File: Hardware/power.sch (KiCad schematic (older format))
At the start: 63 parts, among them IC2 SIP32431DR3-T1GE3, IC3 SIP32431DR3-T1GE3, J2 614105150721, J3 B2B-XH-A, J4 POWER ON, Q2 FDC638P, Q3 IRLML6244TRPBF, Q4 BSS138, Q5 BSS138, U10 TPS63900DSKR, U8 TP4056

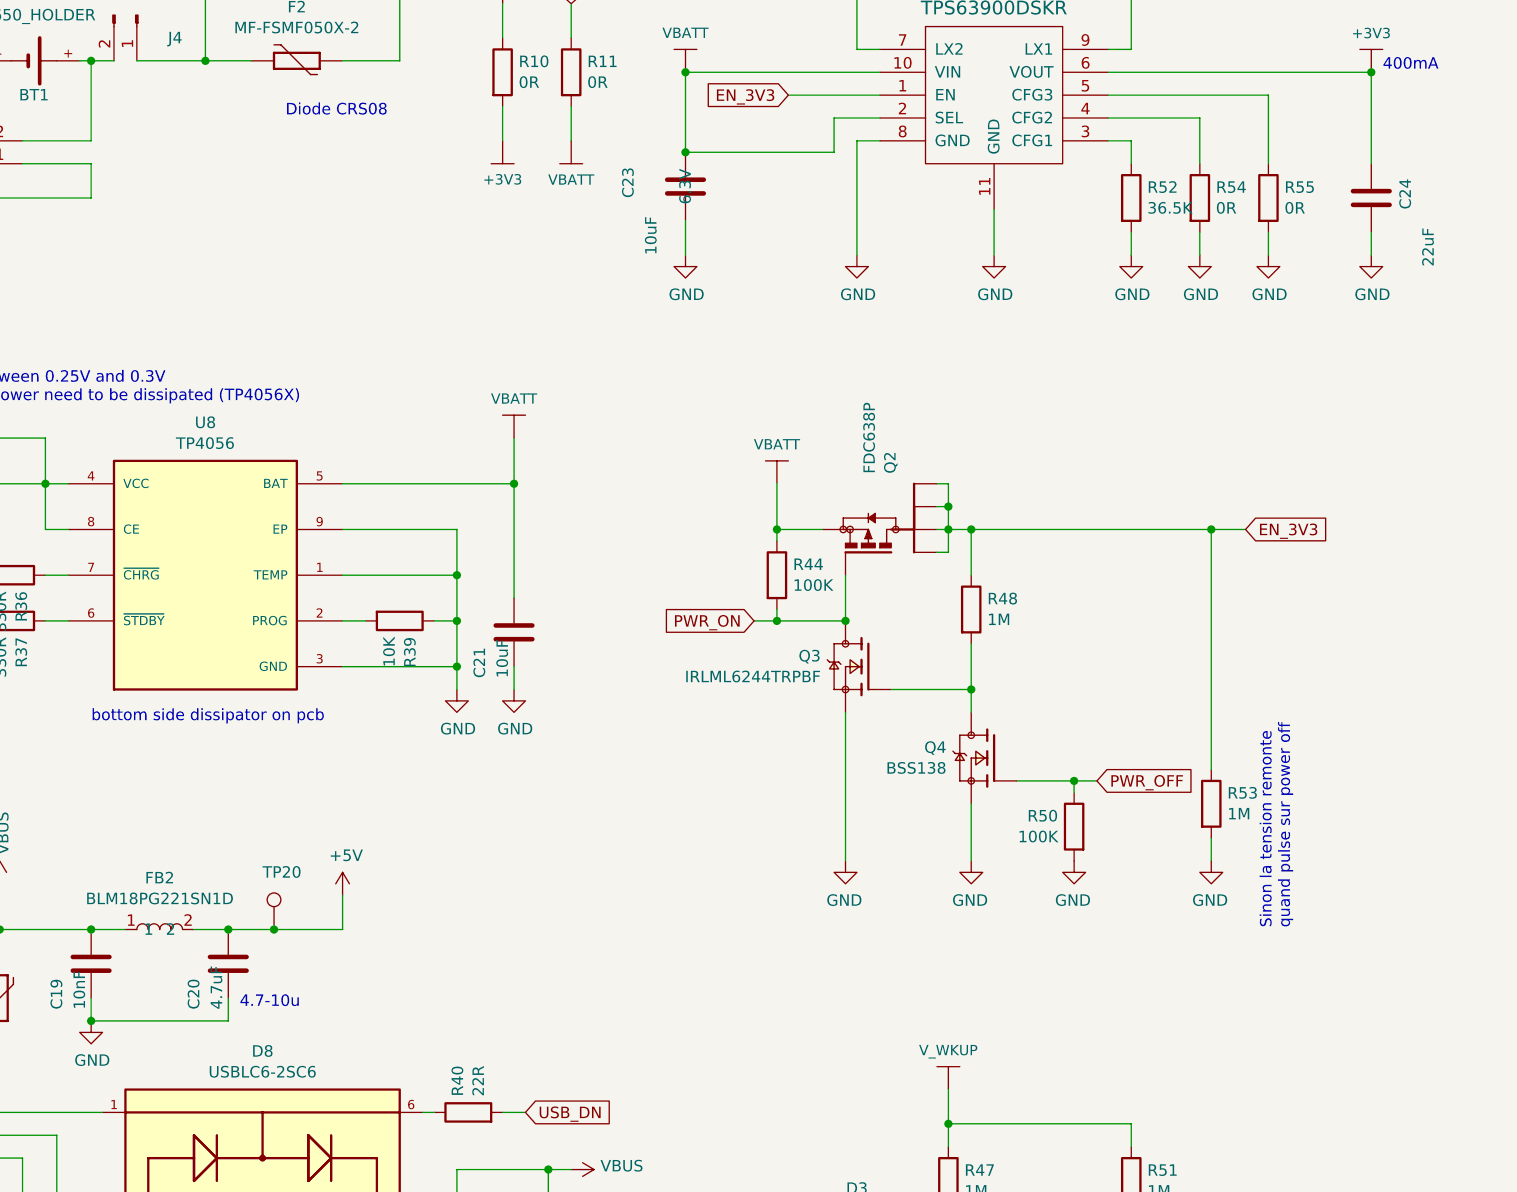
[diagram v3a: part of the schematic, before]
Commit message: Add Gerber files, Bom, Jlcpcb LCSC parts ref, some optimizations
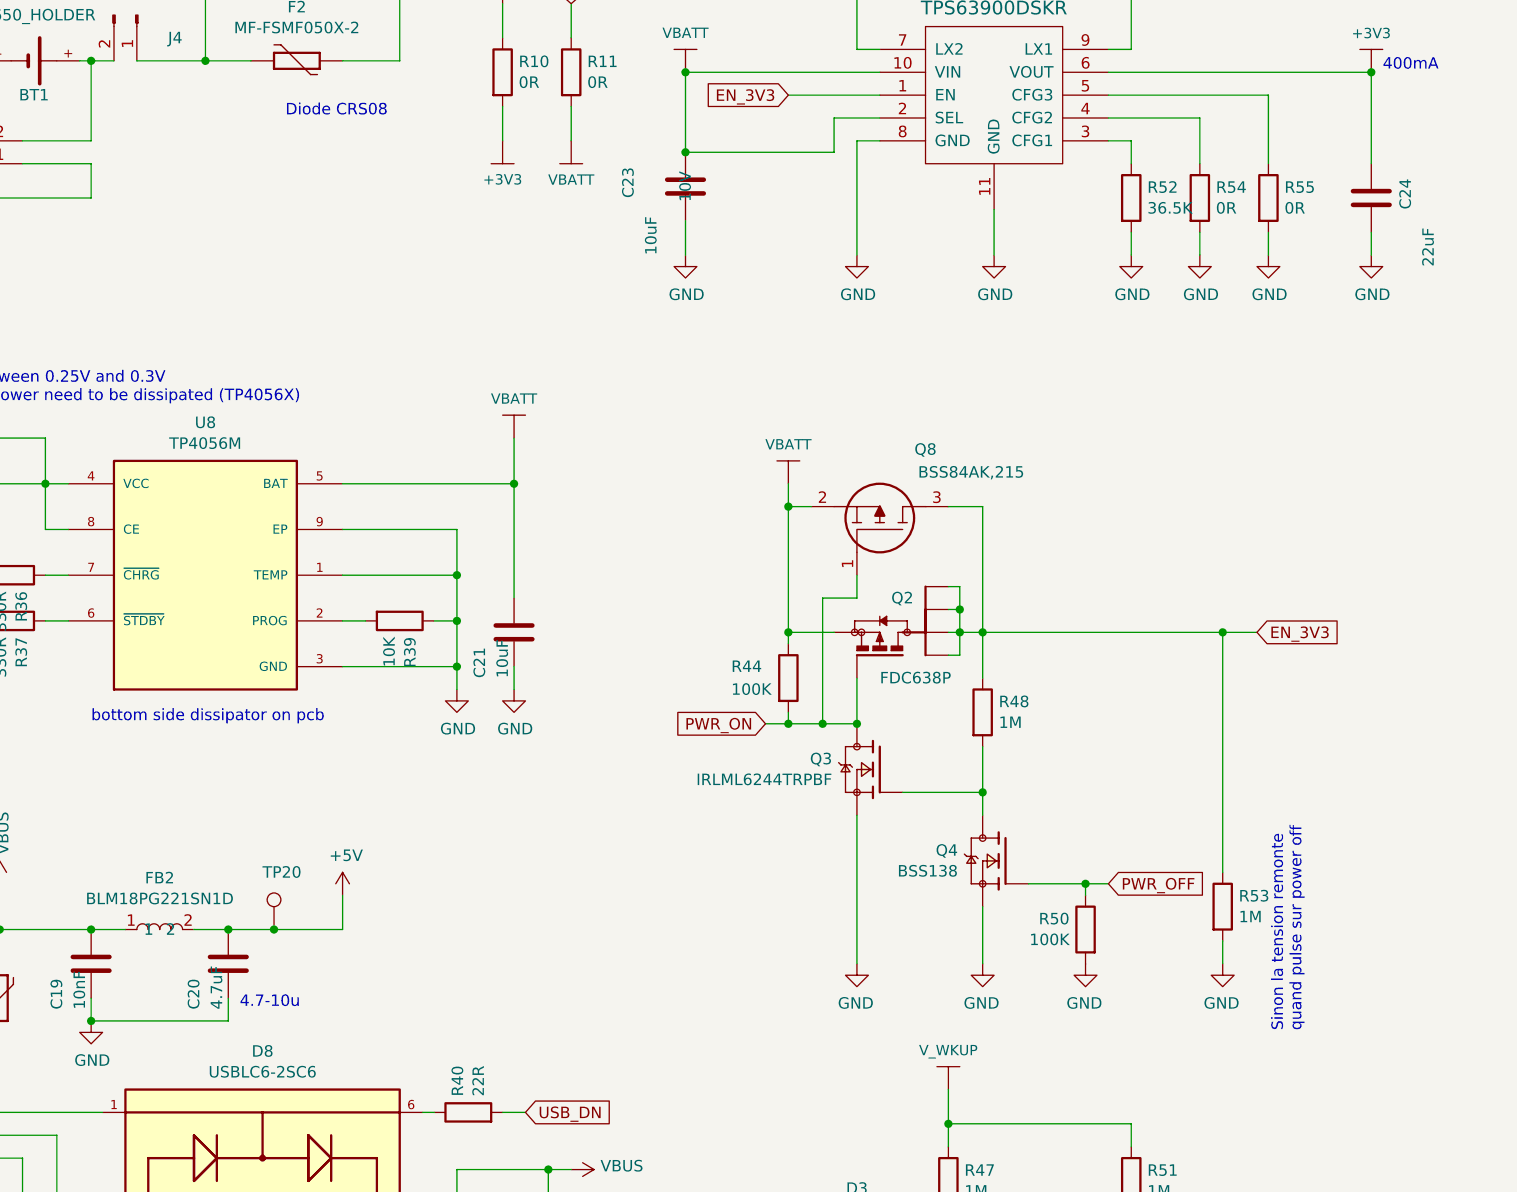
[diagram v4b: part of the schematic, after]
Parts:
- added Q8: BSS84AK,215, EcoApi_pcb:SOT95P230X110-3N, symbol EcoApi_pcb:BSS84AK,215
- C16, C21: Dielectric (none) -> X5R; JLC (none) -> 0603; LCSC (none) -> C19702; Manufacturer_Name (none) -> Samsung Electro-Mechanics; Manufacturer_Part_Number (none) -> CL10A106KP8NNNC; Tolerance (none) -> 10%; Voltage (none) -> 10V
- C17, C20: Dielectric (none) -> X5R; JLC (none) -> 0603; LCSC (none) -> C19666; Manufacturer_Name (none) -> Samsung Electro-Mechanics; Manufacturer_Part_Number (none) -> CL10A475KO8NNNC; Tolerance (none) -> 10%; Voltage (none) -> 16V
- C19: Dielectric (none) -> X7R; JLC (none) -> 0603; LCSC (none) -> C100042; Manufacturer_Name (none) -> Samsung Electro-Mechanics; Manufacturer_Part_Number (none) -> CL10B103KB8NNNC; Tolerance (none) -> 10%; Voltage (none) -> 50V
- C22, C29, C44: Dielectric (none) -> X7R; JLC (none) -> 0603; LCSC (none) -> C1591; Manufacturer_Name (none) -> Samsung Electro-Mechanics; Manufacturer_Part_Number (none) -> CL10B104KB8NNNC; Tolerance (none) -> 10%; Voltage (none) -> 50V
- C23: JLC (none) -> 0603; LCSC (none) -> C19702; Manufacturer_Name (none) -> Samsung Electro-Mechanics; Manufacturer_Part_Number (none) -> CL10A106KP8NNNC; Tolerance (none) -> 10%; Voltage 6.3V -> 10V
- C24: JLC (none) -> 0603; LCSC (none) -> C59461; Manufacturer_Name (none) -> Samsung Electro-Mechanics; Manufacturer_Part_Number (none) -> CL10A226MQ8NRNC; Populate yes -> no; Tolerance (none) -> 20%
- C26, C28: Dielectric (none) -> X7R; JLC (none) -> 0603; LCSC (none) -> C59782; Manufacturer_Name (none) -> Samsung Electro-Mechanics; Manufacturer_Part_Number (none) -> CL10B105KO8NNNC; Tolerance (none) -> 10%
- C27, C45: Dielectric X5R -> X7R; JLC (none) -> 0603; LCSC (none) -> C59782; Manufacturer_Name (none) -> Samsung Electro-Mechanics; Manufacturer_Part_Number (none) -> CL10B105KO8NNNC; Tolerance (none) -> 10%
- D1, D2: Populate yes -> no
- D3, D4, D5, D6: JLC (none) -> SOD-523; LCSC (none) -> C232841; Manufacturer_Name (none) -> onsemi; Manufacturer_Part_Number (none) -> 1N4148WT; package (none) -> SOD-523
- D8: JLC (none) -> SOT-23-6; LCSC (none) -> C7519; Manufacturer_Name (none) -> STMicroelectronics; Manufacturer_Part_Number (none) -> USBLC6-2SC6
- F1, F2: JLC (none) -> 0603; LCSC (none) -> C210357; Manufacturer_Name (none) -> BOURNS; Manufacturer_Part_Number (none) -> MF-FSMF050X-2; Size Inch (none) -> 0603; Size Metric (none) -> 1608
- FB1, FB2: JLC (none) -> 0603; LCSC (none) -> C80165
- IC2, IC3: JLC (none) -> SC-70-6; LCSC (none) -> C141606
- L2: JLC (none) -> 0603; Populate yes -> no
- PS1: JLC (none) -> SOT-23-5; LCSC (none) -> C892187; package (none) -> SOT-23-5
- Q2: JLC (none) -> SSOT-6; Populate yes -> no
- Q3: JLC (none) -> SOT-23-3; LCSC (none) -> C143946
- Q4, Q5: JLC (none) -> SOT-323-3; LCSC (none) -> C24553; Manufacturer_Name onsemi -> Diodes Incorporated; Manufacturer_Part_Number BSS138 -> BSS138W-7-F; package SOT-23-3 -> SOT-323-3
- R10: JLC (none) -> 1206; LCSC (none) -> C17888; Manufacturer_Name (none) -> UNI-ROYAL(Uniroyal Elec); Manufacturer_Part_Number (none) -> 1206W4F0000T5E; Power Rating (none) -> 1/4W; Voltage (none) -> 200V
- R11, R12, R13, R49: JLC (none) -> 0603; LCSC (none) -> C21189; Manufacturer_Name (none) -> UNI-ROYAL(Uniroyal Elec); Manufacturer_Part_Number (none) -> 0603WAF0000T5E; Power Rating (none) -> 1/10W; Voltage (none) -> 75V
- R34, R47, R48, R51, R53: JLC (none) -> 0603; LCSC (none) -> C22935; Manufacturer_Name (none) -> UNI-ROYAL(Uniroyal Elec); Manufacturer_Part_Number (none) -> 0603WAF1004T5E; Power Rating (none) -> 1/10W; Voltage (none) -> 75V
- R35: JLC (none) -> 2512; LCSC (none) -> C27777; Manufacturer_Name (none) -> UNI-ROYAL(Uniroyal Elec); Manufacturer_Part_Number (none) -> 25121WF500LT4E; Power Rating 2W -> 1W; Size Inch 6332 -> 2512; Size Metric 2512 -> 6332; Voltage (none) -> 200V
- R36, R37: JLC (none) -> 0603; LCSC (none) -> C23138; Manufacturer_Name (none) -> UNI-ROYAL(Uniroyal Elec); Manufacturer_Part_Number (none) -> 0603WAF3300T5E; Power Rating (none) -> 1/10W; Voltage (none) -> 75V
- R38, R44, R50: JLC (none) -> 0603; LCSC (none) -> C25803; Manufacturer_Name (none) -> UNI-ROYAL(Uniroyal Elec); Manufacturer_Part_Number (none) -> 0603WAF1003T5E; Power Rating (none) -> 1/10W; Voltage (none) -> 75V
- R39: JLC (none) -> 0603; LCSC (none) -> C25804; Manufacturer_Name (none) -> UNI-ROYAL(Uniroyal Elec); Manufacturer_Part_Number (none) -> 0603WAF1002T5E; Power Rating (none) -> 1/10W; Voltage (none) -> 75V
- R40, R41: JLC (none) -> 0603; LCSC (none) -> C23345; Manufacturer_Name (none) -> UNI-ROYAL(Uniroyal Elec); Manufacturer_Part_Number (none) -> 0603WAF220JT5E; Power Rating (none) -> 1/10W; Voltage (none) -> 75V
- R52: JLC (none) -> 0603; LCSC (none) -> C51261; Manufacturer_Name (none) -> UNI-ROYAL(Uniroyal Elec); Manufacturer_Part_Number (none) -> TC0325D3652T5E; Populate yes -> no; Power Rating (none) -> 1/16W; Tolerance 1% -> 0.5%; Voltage (none) -> 75V
- R54, R55: JLC (none) -> 0603; LCSC (none) -> C21189; Manufacturer_Name (none) -> UNI-ROYAL(Uniroyal Elec); Manufacturer_Part_Number (none) -> 0603WAF0000T5E; Populate yes -> no; Power Rating (none) -> 1/10W; Voltage (none) -> 75V
- U8: value TP4056 -> TP4056M; JLC (none) -> SOP-8; LCSC (none) -> C21417; Manufacturer_Part_Number TP4056 -> TP4056M
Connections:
- net EN_3V3: now also Q8.3
- net PWR_ON: now also Q8.1
- net VBATT: now also Q8.2
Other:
- moved on the sheet: Q2, Q3, Q4, R44, R48, R50, R53

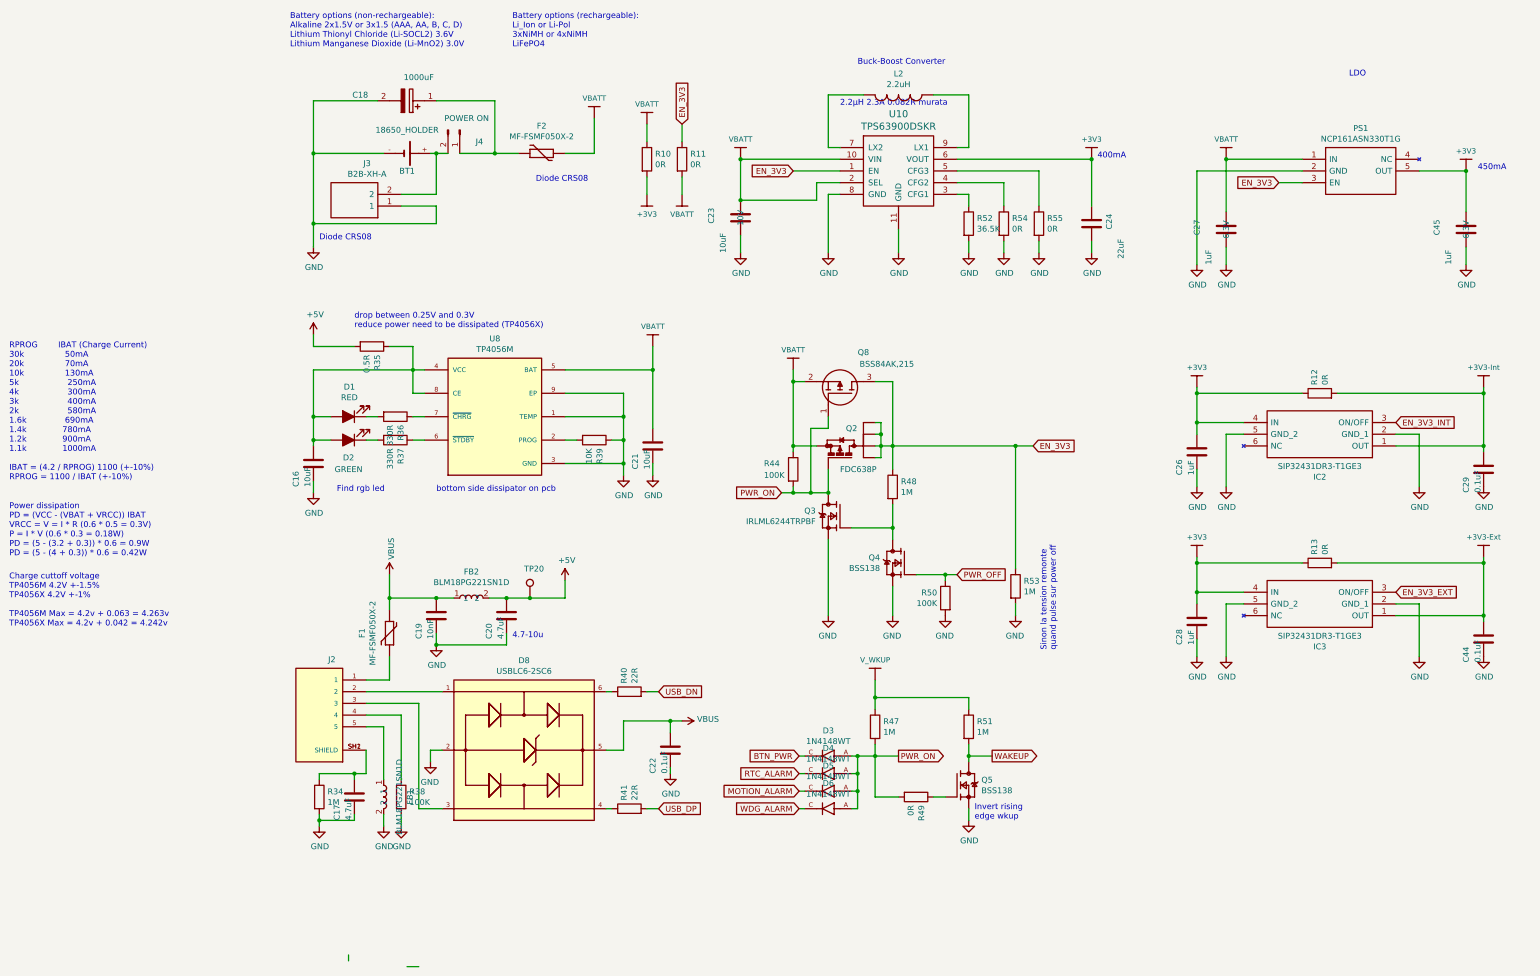
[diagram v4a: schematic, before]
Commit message: Fix JLCPCB assembly issues, Add reverse battery protection, Define Correct crystal capa, Add Layer number and fiducial, and some quicq fix
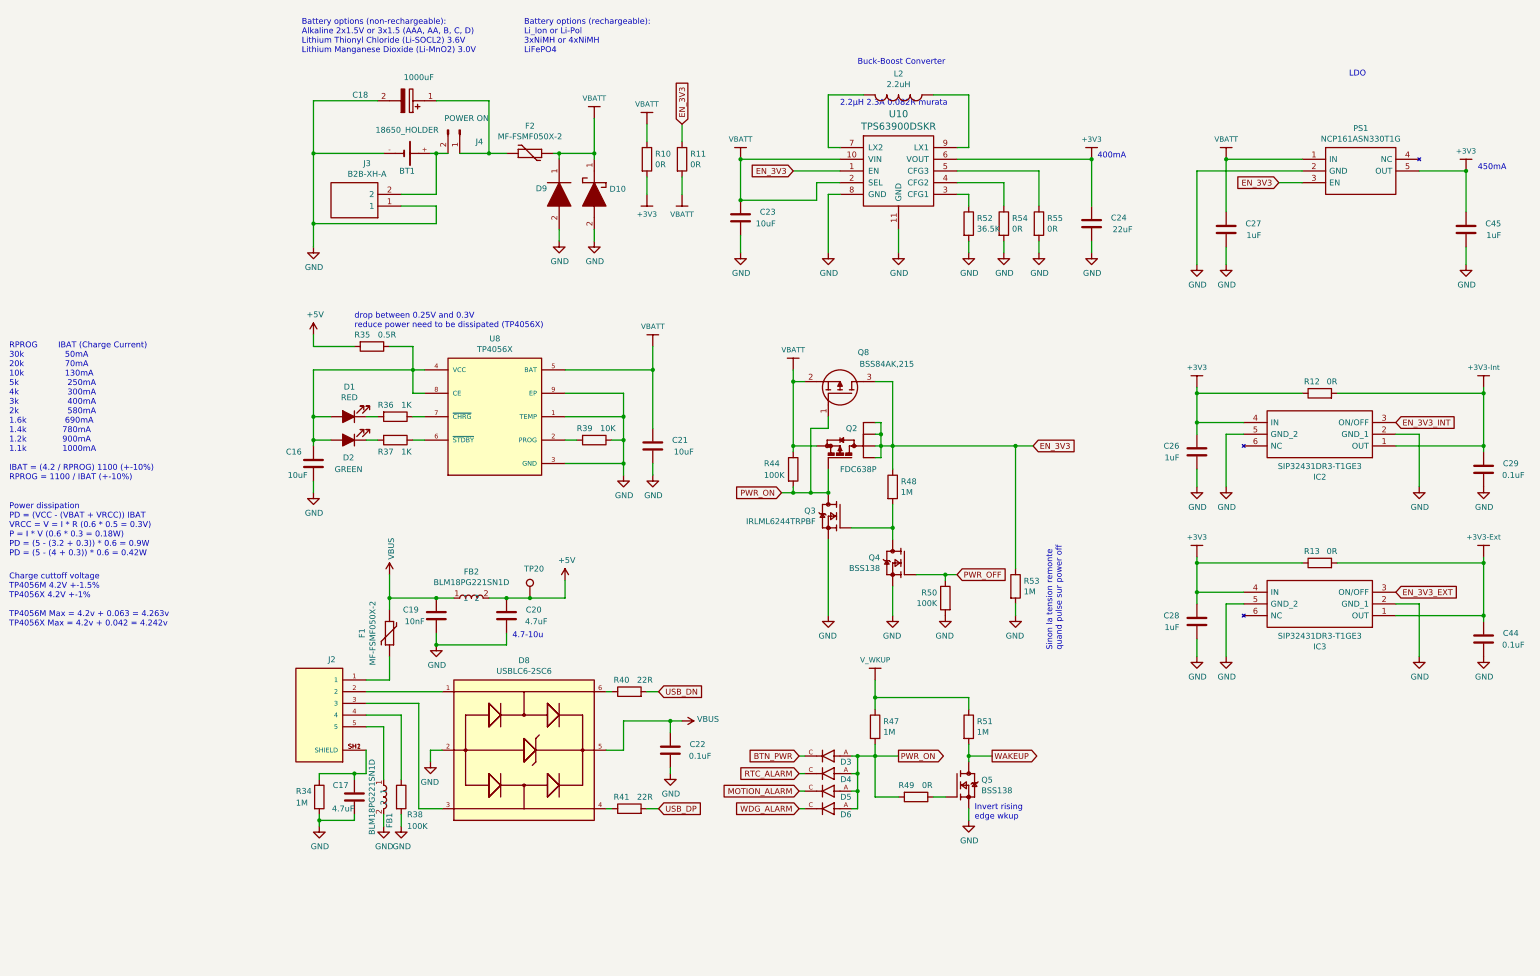
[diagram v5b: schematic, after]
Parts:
- added D10: PMEG10020AELPX, EcoApi_pcb:SODFL4725X110N, symbol EcoApi_pcb:PMEG10020AELPX
- added D9: PMEG10010ELRX, EcoApi_pcb:SOD123_Generic(W_F_FL), symbol EcoApi_pcb:PMEG10010ELRX
- C23: LCSC C19702 -> NM_C19702; Populate yes -> no
- C24: LCSC C59461 -> NM_C59461
- Q4, Q5: footprint EcoApi_pcb:SOT95P240X111-3N -> EcoApi_pcb:SOT65P210X110-3N
- R10: LCSC C17888 -> NM_C17888
- R11, R12, R13, R54, R55: LCSC C21189 -> NM_C21189
- R36, R37: value 330R -> 1K; LCSC C23138 -> C21190; Manufacturer_Part_Number 0603WAF3300T5E -> 0603WAF1001T5E
- R52: LCSC C51261 -> NM_C51261_
- U8: value TP4056M -> TP4056X; LCSC C21417 -> C2763448; Manufacturer_Part_Number TP4056M -> TP4056X-42-ESOP8
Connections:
- net GND: now also D10.2, D9.2
- net VBATT: now also D10.1, D9.1
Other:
- note removed: "Diode CRS08"
- note removed: "Find rgb led"
- note removed: "bottom side dissipator on pcb"
- moved on the sheet: F2

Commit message: Debug some features on hardware
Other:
- note added: "Revoir avec eval kit la partie switch low power\nVoir TPS22917"
- note added: "Voir pull down sur signal on off"
- note added: "enlever wdg alarm"
- note added: "voir si pas autre car introuvable"
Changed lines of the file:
@@
 Wire Wire Line
 	2850 2400 2850 2500
+Text Notes 8750 4900 0    50   ~ 0
+Voir pull down sur signal on off
+Text Notes 5200 850  0    50   ~ 0
+voir si pas autre car introuvable
+Text Notes 4550 7600 0    50   ~ 0
+enlever wdg alarm
+Text Notes 8650 3550 0    50   ~ 0
+Revoir avec eval kit la partie switch low power\nVoir TPS22917
 $EndSCHEMATC

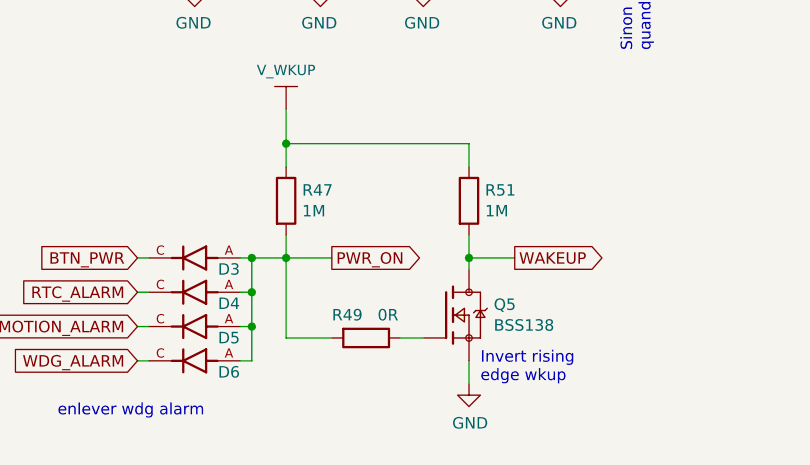
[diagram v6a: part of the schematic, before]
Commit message: Fix motion detection, validation done for usb solar charger
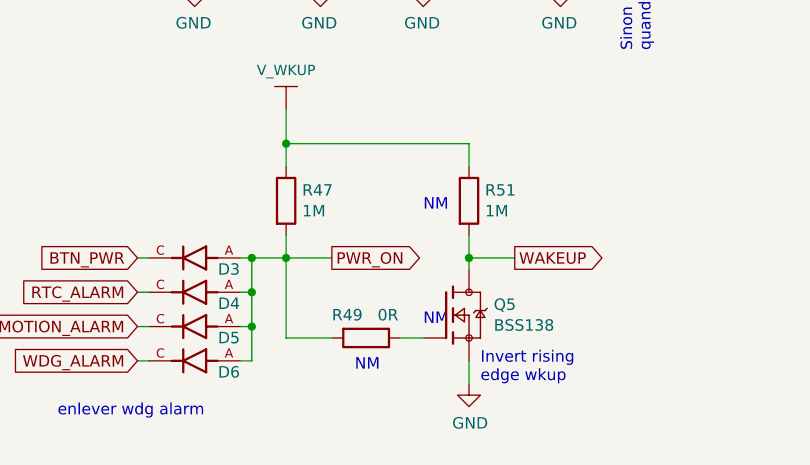
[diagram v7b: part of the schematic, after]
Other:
- note added: "NM"
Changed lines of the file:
@@
 Text Notes 8650 3550 0    50   ~ 0
 Revoir avec eval kit la partie switch low power\nVoir TPS22917
+Text Notes 6150 6700 0    50   ~ 0
+NM
+Text Notes 5850 7400 0    50   ~ 0
+NM
+Text Notes 6150 7200 0    50   ~ 0
+NM
 $EndSCHEMATC
